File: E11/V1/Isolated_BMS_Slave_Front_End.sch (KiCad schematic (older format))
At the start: 26 parts, among them J501 64900221122, Q501 CPH6347-TL-W, Q502 CPH6347-TL-W, U501 LTV-816S, U502 SI8641AB-B-IS1

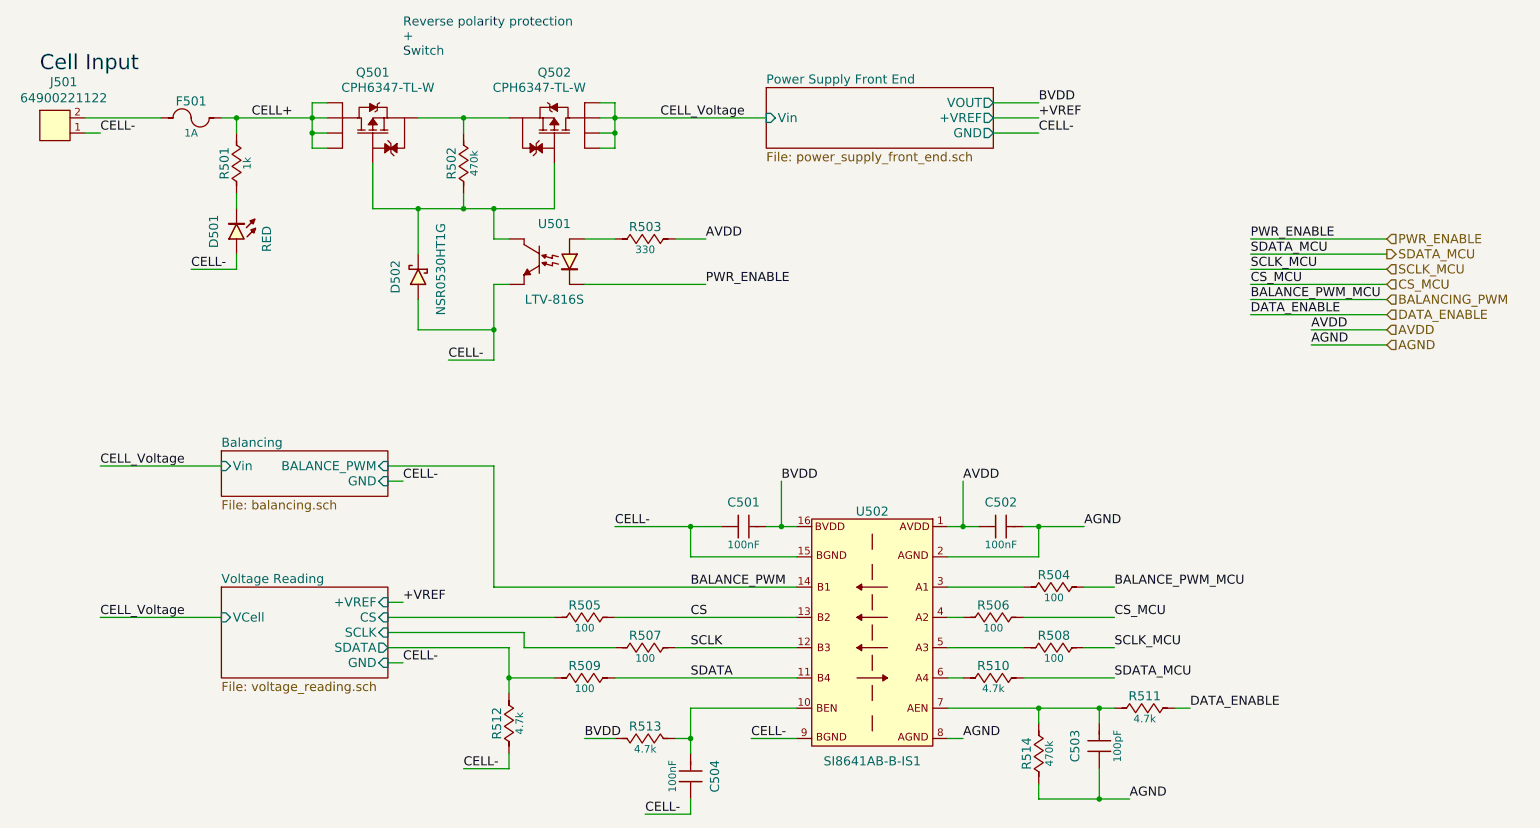
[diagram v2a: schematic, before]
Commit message: updated filter values and pcb
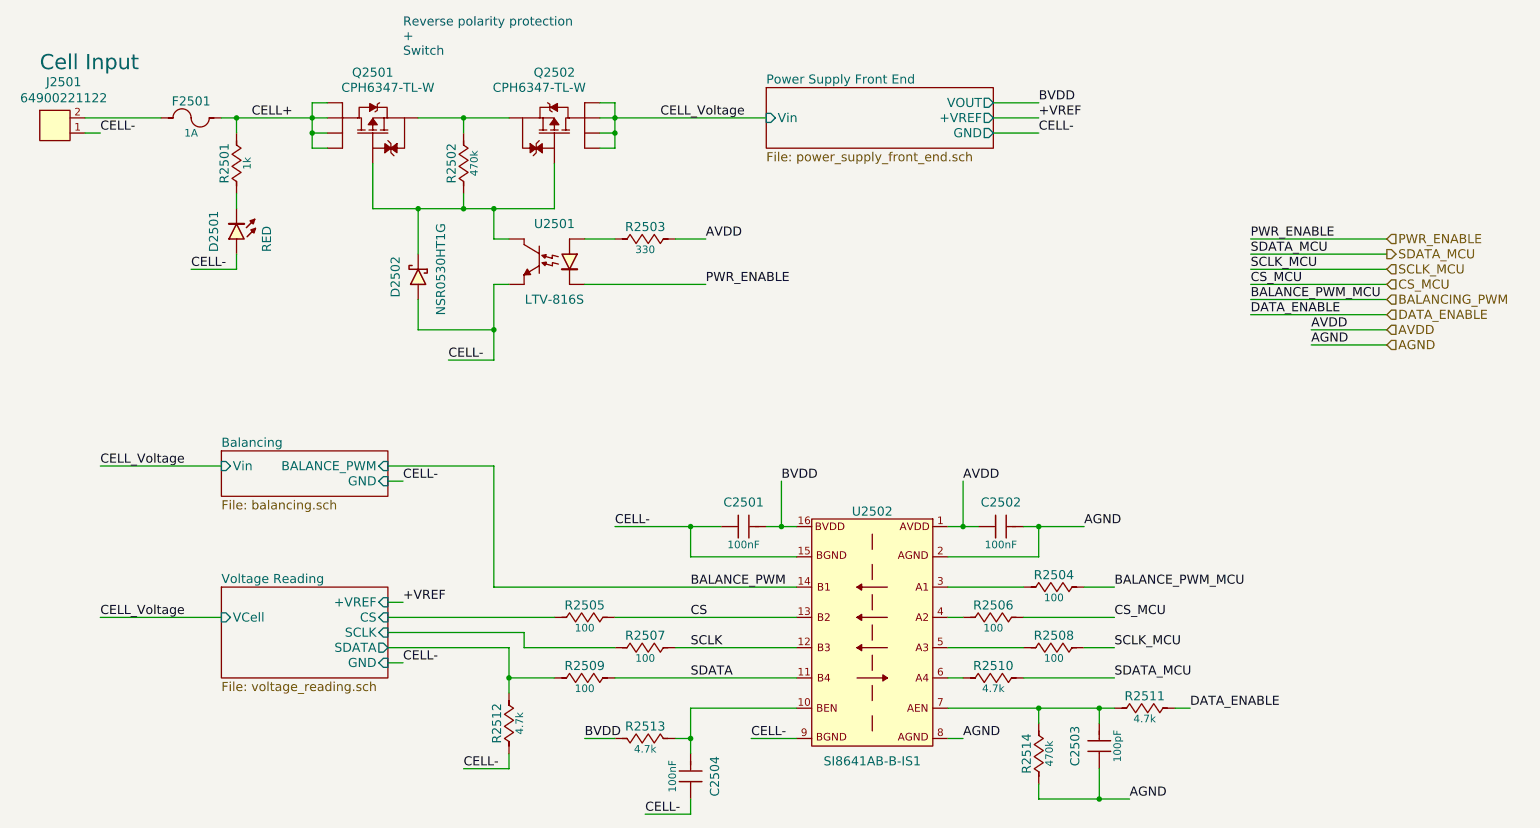
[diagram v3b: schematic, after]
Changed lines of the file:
@@
 $Descr USLetter 11000 8500
 encoding utf-8
-Sheet 5 28
+Sheet 25 28
 Title "Isolated BMS Slave Front End"
 Date ""
@@
 AR Path="/59400152/591B47DF" Ref="Q2501"  Part="1"
 AR Path="/59400D56/591B47DF" Ref="Q2901"  Part="1"
-F 0 "Q501" V 3300 1300 60  0000 C CNN
+F 0 "Q2501" V 3300 1300 60  0000 C CNN
 F 1 "CPH6347-TL-W" V 3200 1200 60  0000 C CNN
 F 2 "IC:TSOT-23-6" H 3000 400 60  0001 C CNN
@@
 AR Path="/59400D56/591D60B1" Ref="U2902"  Part="1"
 AR Path="/591D60B1" Ref="U502"  Part="1"
-F 0 "U502" H 6200 5400 60  0000 C CNN
+F 0 "U2502" H 6200 5400 60  0000 C CNN
 F 1 "SI8641AB-B-IS1" H 6200 3750 60  0000 C CNN
 F 2 "IC:SOIC-16" H 6200 2800 60  0001 C CNN
@@
 AR Path="/59400152/591D614C" Ref="C2502"  Part="1"
 AR Path="/59400D56/591D614C" Ref="C2902"  Part="1"
-F 0 "C502" H 7050 4060 60  0000 C CNN
+F 0 "C2502" H 7050 4060 60  0000 C CNN
 F 1 "885012206095" H 7050 3550 60  0001 C CNN
 F 2 "Capacitors:C0603" H 7050 2950 60  0001 C CNN
@@
 AR Path="/59400152/591D641D" Ref="C2501"  Part="1"
 AR Path="/59400D56/591D641D" Ref="C2901"  Part="1"
-F 0 "C501" H 5350 4060 60  0000 C CNN
+F 0 "C2501" H 5350 4060 60  0000 C CNN
 F 1 "885012206095" H 5350 3550 60  0001 C CNN
 F 2 "Capacitors:C0603" H 5350 2950 60  0001 C CNN
@@
 AR Path="/59400152/591D91BB" Ref="R2513"  Part="1"
 AR Path="/59400D56/591D91BB" Ref="R2913"  Part="1"
-F 0 "R513" H 4700 5380 60  0000 C CNN
+F 0 "R2513" H 4700 5380 60  0000 C CNN
 F 1 "RC0603JR-074K7L" H 4700 5000 50  0001 C CNN
 F 2 "Resistors:R0603" H 4700 4400 30  0001 C CNN
@@
 AR Path="/59400152/591D91D0" Ref="C2504"  Part="1"
 AR Path="/59400D56/591D91D0" Ref="C2904"  Part="1"
-F 0 "C504" H 4950 5660 60  0000 C CNN
+F 0 "C2504" H 4950 5660 60  0000 C CNN
 F 1 "885012206095" H 4950 5150 60  0001 C CNN
 F 2 "Capacitors:C0603" H 4950 4550 60  0001 C CNN
@@
 AR Path="/59400152/5938F00C" Ref="Q2502"  Part="1"
 AR Path="/59400D56/5938F00C" Ref="Q2902"  Part="1"
-F 0 "Q502" V 4500 1300 60  0000 C CNN
+F 0 "Q2502" V 4500 1300 60  0000 C CNN
 F 1 "CPH6347-TL-W" V 4400 1200 60  0000 C CNN
 F 2 "IC:TSOT-23-6" H 4200 400 60  0001 C CNN
@@
 AR Path="/59400152/593917FE" Ref="R2512"  Part="1"
 AR Path="/59400D56/593917FE" Ref="R2912"  Part="1"
-F 0 "R512" H 3800 5280 60  0000 C CNN
+F 0 "R2512" H 3800 5280 60  0000 C CNN
 F 1 "RC0603JR-074K7L" H 3800 4900 50  0001 C CNN
 F 2 "Resistors:R0603" H 3800 4300 30  0001 C CNN
@@
 AR Path="/59400152/593919F1" Ref="R2509"  Part="1"
 AR Path="/59400D56/593919F1" Ref="R2909"  Part="1"
-F 0 "R509" H 4300 4980 60  0000 C CNN
+F 0 "R2509" H 4300 4980 60  0000 C CNN
 F 1 "RC0603FR-07100RL" H 4300 4600 50  0001 C CNN
 F 2 "Resistors:R0603" H 4300 4000 30  0001 C CNN
@@
 AR Path="/59400152/59391AB0" Ref="R2507"  Part="1"
 AR Path="/59400D56/59391AB0" Ref="R2907"  Part="1"
-F 0 "R507" H 4700 4780 60  0000 C CNN
+F 0 "R2507" H 4700 4780 60  0000 C CNN
 F 1 "RC0603FR-07100RL" H 4700 4400 50  0001 C CNN
 F 2 "Resistors:R0603" H 4700 3800 30  0001 C CNN
@@
 AR Path="/59400152/59391AED" Ref="R2505"  Part="1"
 AR Path="/59400D56/59391AED" Ref="R2905"  Part="1"
-F 0 "R505" H 4300 4580 60  0000 C CNN
+F 0 "R2505" H 4300 4580 60  0000 C CNN
 F 1 "RC0603FR-07100RL" H 4300 4200 50  0001 C CNN
 F 2 "Resistors:R0603" H 4300 3600 30  0001 C CNN
@@
 AR Path="/59400D56/59395C7C" Ref="U2901"  Part="1"
 AR Path="/59395C7C" Ref="U501"  Part="1"
-F 0 "U501" H 4100 2500 60  0000 C CNN
+F 0 "U2501" H 4100 2500 60  0000 C CNN
 F 1 "LTV-816S" H 4100 2000 60  0000 C CNN
 F 2 "IC:4-SMD" H 4100 1300 60  0001 C CNN
@@
 AR Path="/59400152/59396188" Ref="R2503"  Part="1"
 AR Path="/59400D56/59396188" Ref="R2903"  Part="1"
-F 0 "R503" H 4700 2080 60  0000 C CNN
+F 0 "R2503" H 4700 2080 60  0000 C CNN
 F 1 "RC0603JR-07330RL" H 4700 1700 50  0001 C CNN
 F 2 "Resistors:R0603" H 4700 1100 30  0001 C CNN
@@
 AR Path="/59400152/5939743F" Ref="D2502"  Part="1"
 AR Path="/59400D56/5939743F" Ref="D2902"  Part="1"
-F 0 "D502" H 3150 2350 60  0000 C CNN
+F 0 "D2502" H 3150 2350 60  0000 C CNN
 F 1 "NSR0530HT1G" H 3200 2050 60  0000 C CNN
 F 2 "Diodes:SOD-323" H 3180 1200 60  0001 C CNN
@@
 AR Path="/59400152/5939A33B" Ref="C2503"  Part="1"
 AR Path="/59400D56/5939A33B" Ref="C2903"  Part="1"
-F 0 "C503" H 7650 5460 60  0000 C CNN
+F 0 "C2503" H 7650 5460 60  0000 C CNN
 F 1 "885012206077" H 7650 4950 60  0001 C CNN
 F 2 "Capacitors:C0603" H 7650 4350 60  0001 C CNN
@@
 AR Path="/59400152/59397104" Ref="R2502"  Part="1"
 AR Path="/59400D56/59397104" Ref="R2902"  Part="1"
-F 0 "R502" H 3500 1580 60  0000 C CNN
+F 0 "R2502" H 3500 1580 60  0000 C CNN
 F 1 "RC0603JR-07470KL" H 3500 1200 50  0001 C CNN
 F 2 "Resistors:R0603" H 3500 600 30  0001 C CNN
@@
 AR Path="/59400D56/593A1551" Ref="D2901"  Part="1"
 AR Path="/593A1551" Ref="D2101"  Part="1"
-F 0 "D501" H 1950 2050 60  0000 C CNN
+F 0 "D2501" H 1950 2050 60  0000 C CNN
 F 1 "150080RS75000" H 2000 1700 60  0001 C CNN
 F 2 "Diodes:LED_0805_RED" H 2010 820 60  0001 C CNN
@@
 AR Path="/59400152/593A2339" Ref="R2501"  Part="1"
 AR Path="/59400D56/593A2339" Ref="R2901"  Part="1"
-F 0 "R501" H 2000 1580 60  0000 C CNN
+F 0 "R2501" H 2000 1580 60  0000 C CNN
 F 1 "RC0603JR-071KL" H 2000 1200 50  0001 C CNN
 F 2 "Resistors:R0603" H 2000 600 30  0001 C CNN
@@
 AR Path="/59400152/593D0FB3" Ref="R2510"  Part="1"
 AR Path="/59400D56/593D0FB3" Ref="R2910"  Part="1"
-F 0 "R510" H 7000 4980 60  0000 C CNN
+F 0 "R2510" H 7000 4980 60  0000 C CNN
 F 1 "RC0603JR-074K7L" H 7000 4600 50  0001 C CNN
 F 2 "Resistors:R0603" H 7000 4000 30  0001 C CNN
@@
 AR Path="/59400152/593D1688" Ref="R2511"  Part="1"
 AR Path="/59400D56/593D1688" Ref="R2911"  Part="1"
-F 0 "R511" H 8000 5180 60  0000 C CNN
+F 0 "R2511" H 8000 5180 60  0000 C CNN
 F 1 "RC0603JR-074K7L" H 8000 4800 50  0001 C CNN
 F 2 "Resistors:R0603" H 8000 4200 30  0001 C CNN
@@
 AR Path="/59400152/593D16CF" Ref="R2514"  Part="1"
 AR Path="/59400D56/593D16CF" Ref="R2914"  Part="1"
-F 0 "R514" H 7300 5480 60  0000 C CNN
+F 0 "R2514" H 7300 5480 60  0000 C CNN
 F 1 "RC0603JR-07470KL" H 7300 5100 50  0001 C CNN
 F 2 "Resistors:R0603" H 7300 4500 30  0001 C CNN
@@
 AR Path="/59400152/593934E8" Ref="R2508"  Part="1"
 AR Path="/59400D56/593934E8" Ref="R2908"  Part="1"
-F 0 "R508" H 7400 4780 60  0000 C CNN
+F 0 "R2508" H 7400 4780 60  0000 C CNN
 F 1 "RC0603FR-07100RL" H 7400 4400 50  0001 C CNN
 F 2 "Resistors:R0603" H 7400 3800 30  0001 C CNN
@@
 AR Path="/59400152/593932C5" Ref="R2506"  Part="1"
 AR Path="/59400D56/593932C5" Ref="R2906"  Part="1"
-F 0 "R506" H 7000 4580 60  0000 C CNN
+F 0 "R2506" H 7000 4580 60  0000 C CNN
 F 1 "RC0603FR-07100RL" H 7000 4200 50  0001 C CNN
 F 2 "Resistors:R0603" H 7000 3600 30  0001 C CNN
@@
 AR Path="/59400152/59392BA0" Ref="R2504"  Part="1"
 AR Path="/59400D56/59392BA0" Ref="R2904"  Part="1"
-F 0 "R504" H 7400 4380 60  0000 C CNN
+F 0 "R2504" H 7400 4380 60  0000 C CNN
 F 1 "RC0603FR-07100RL" H 7400 4000 50  0001 C CNN
 F 2 "Resistors:R0603" H 7400 3400 30  0001 C CNN
@@
 AR Path="/59400D56/5948E47C" Ref="F2901"  Part="1"
 AR Path="/59400D60/5948E47C" Ref="F3301"  Part="1"
-F 0 "F501" H 1700 1310 60  0000 C CNN
+F 0 "F2501" H 1700 1310 60  0000 C CNN
 F 1 "39511000440" H 1700 900 50  0001 C CNN
 F 2 "Fuses:TE5_395" H 1700 300 30  0001 C CNN
@@
 AR Path="/593FF93E/5EBA09D2" Ref="J2101"  Part="1"
 AR Path="/59400152/5EBA09D2" Ref="J2501"  Part="1"
-F 0 "J501" H 858 1637 60  0000 C CNN
+F 0 "J2501" H 858 1637 60  0000 C CNN
 F 1 "64900221122" H 858 1531 60  0000 C CNN
 F 2 "Connectors:64900221122" H 800 400 60  0001 C CNN
